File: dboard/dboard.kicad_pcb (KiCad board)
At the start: 2 copper layers, 53 x 24 mm, 29 parts, among them J1 Conn_01x04, J2 Conn_01x04, U1 SRV05-4, U2 SRV05-4

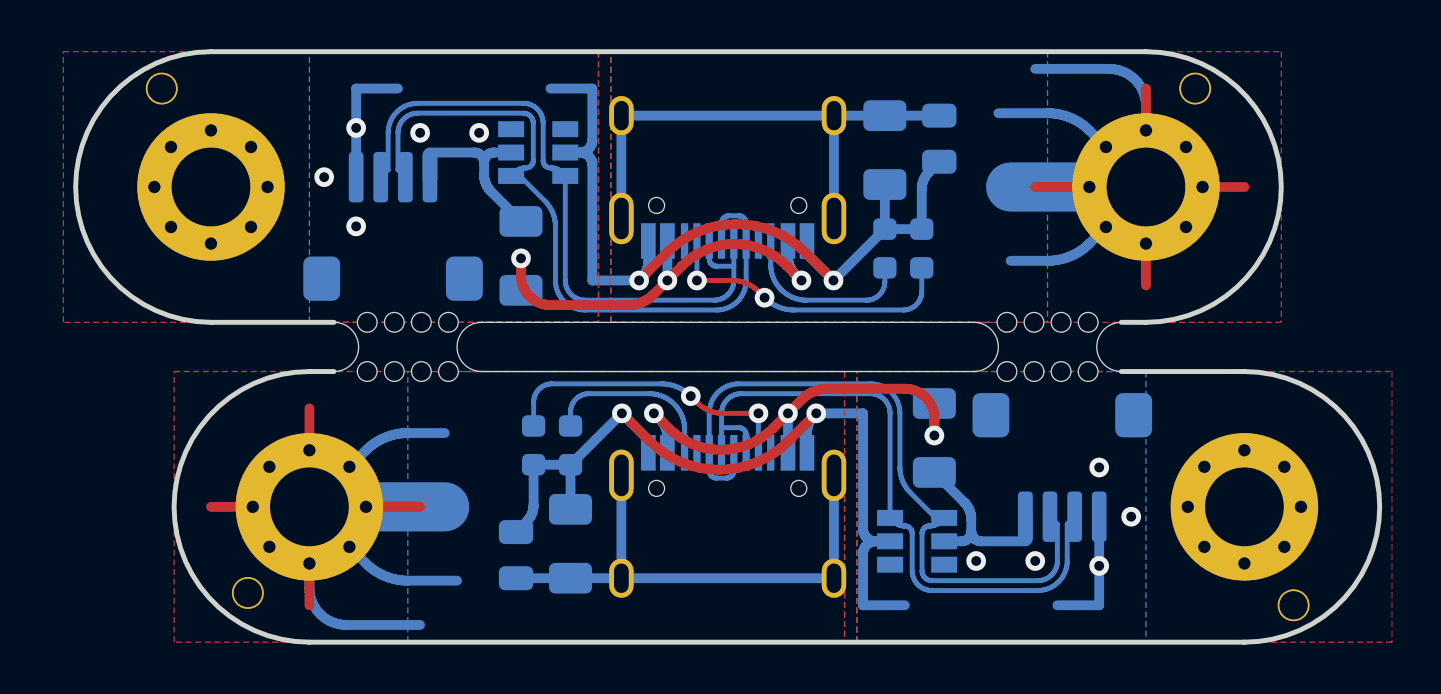
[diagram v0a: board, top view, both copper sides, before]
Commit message: separated jlc files
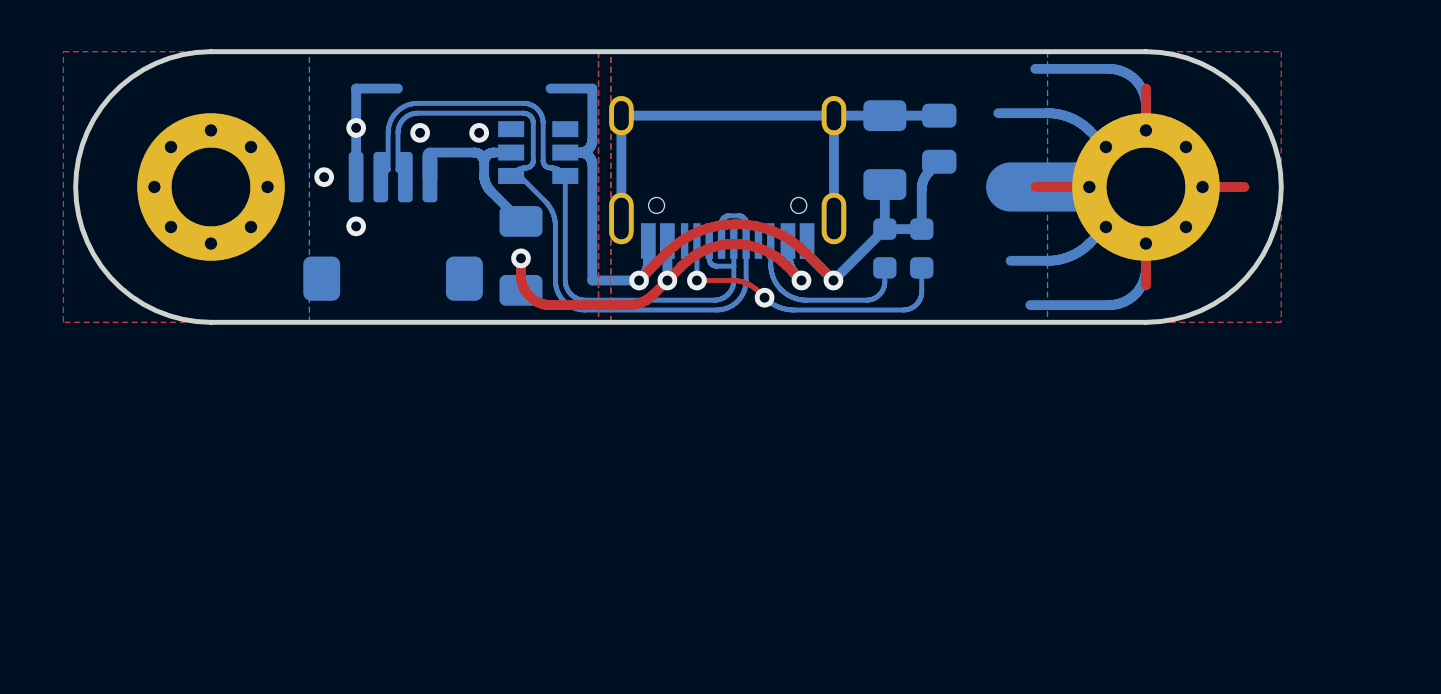
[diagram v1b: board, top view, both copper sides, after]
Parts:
- removed C2: 470n, Capacitor_SMD:C_0805_2012Metric
- removed F2: 500mA, Fuse:Fuse_1206_3216Metric
- removed H10, H12, H6, H8: mousebites, crokto:mousebites-6mm
- removed H11, H13, H7, H9: pcba, crokto:JLCPCBA
- removed H3: MountingHole, crokto:M3_Via_Hole_NC
- removed H4: MountingHole_Pad, crokto:M3_Via_Hole
- removed H5: jlc, crokto:jlc
- removed J2: Conn_01x04, crokto:JST_SH_SM04B-SRSS-TB_1x04-1MP_P1.00mm_Horizontal
- removed R4, R5: 5.1K, Resistor_SMD:R_0603_1608Metric
- removed R6: 1M, Resistor_SMD:R_1206_3216Metric
- removed U2: SRV05-4, Package_TO_SOT_SMD:SOT-23-6
- removed USB2: HRO-TYPE-C-31-M-12, Type-C:HRO-TYPE-C-31-M-12-Assembly
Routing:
- net SHIELD: track 131.4 -> 74.6 mm
- net GND: track 80.7 -> 40.3 mm, vias 14 -> 7
- net D+: track 58.9 -> 29.5 mm
- net D-: track 55.2 -> 27.6 mm
- net VBUS: track 37.6 -> 18.8 mm, vias 6 -> 3
- net Net-(R4-Pad2): track 12.5 -> 0.00 mm, vias 2 -> 0
- net +5V: track 15.5 -> 7.74 mm
- net Net-(R5-Pad2): track 7.41 -> 0.00 mm
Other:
- board size 53 x 24 mm -> 49 x 11 mm

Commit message: a bunch of new dboards
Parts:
- added D1: D_TVS, Diode_SMD:D_SOD-123F, B.Cu at (-15.6, 2.50)
- H2: moved to B.Cu
- J1: value Conn_01x04 -> JST_SH_SM04B-SRSS-TB_1x04
- USB1: value HRO-TYPE-C-31-M-12 -> HRO-TYPE-C-31-M-14; footprint Type-C:HRO-TYPE-C-31-M-12-Assembly -> Type-C:HRO-TYPE-C-31-M-14
- moved C1 17.2 mm to (-8.54, 1.70), turned to 180 degrees
- moved R3 15.4 mm to (-9.00, 3.80), turned to 180 degrees
- moved U1 5.39 mm to (-11.2, 8.20), turned to 90 degrees
- moved J1 5.21 mm to (-17.0, 11.3)
- moved H2 4.51 mm to (12.5, 5.75), turned to 180 degrees
- moved R1 4.00 mm to (7.70, 4.00)
- moved H1 3.01 mm to (-24.0, 5.75), turned to 180 degrees
- moved R2 1.65 mm to (7.70, 7.00)
- moved F1 1.03 mm to (-7.90, 7.40)
- turned USB1 to 180 degrees
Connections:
- J1 pad 2: D+ -> D-
- J1 pad 3: D- -> D+
- U1 pad 3: D- -> D+
- U1 pad 4: D+ -> D-
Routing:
- net SHIELD: track 74.6 -> 20.3 mm
- net GND: track 40.3 -> 29.1 mm, vias 7 -> 8
- net +5V: track 7.74 -> 15.1 mm
- net Net-(R1-Pad2): track 12.5 -> 17.5 mm
- net VBUS: track 18.8 -> 13.9 mm, vias 3 -> 2
- net D+: track 29.5 -> 24.9 mm
- net D-: track 27.6 -> 24.3 mm
- net Net-(R2-Pad2): track 7.41 -> 9.67 mm
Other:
- board size 49 x 11 mm -> 43.5 x 11.5 mm
- net class Default: clearance 0.2 -> 0.18
- net class Power: clearance 0.2 -> 0.18
- rule trace_clearance: 0.2 -> 0.18
